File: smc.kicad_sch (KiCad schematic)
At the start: 46 parts, among them SW1 SW_Push, SW2 SW_Push, U5 W25Q128JVS, U6 RP2040, Y1 12MHz 20pF

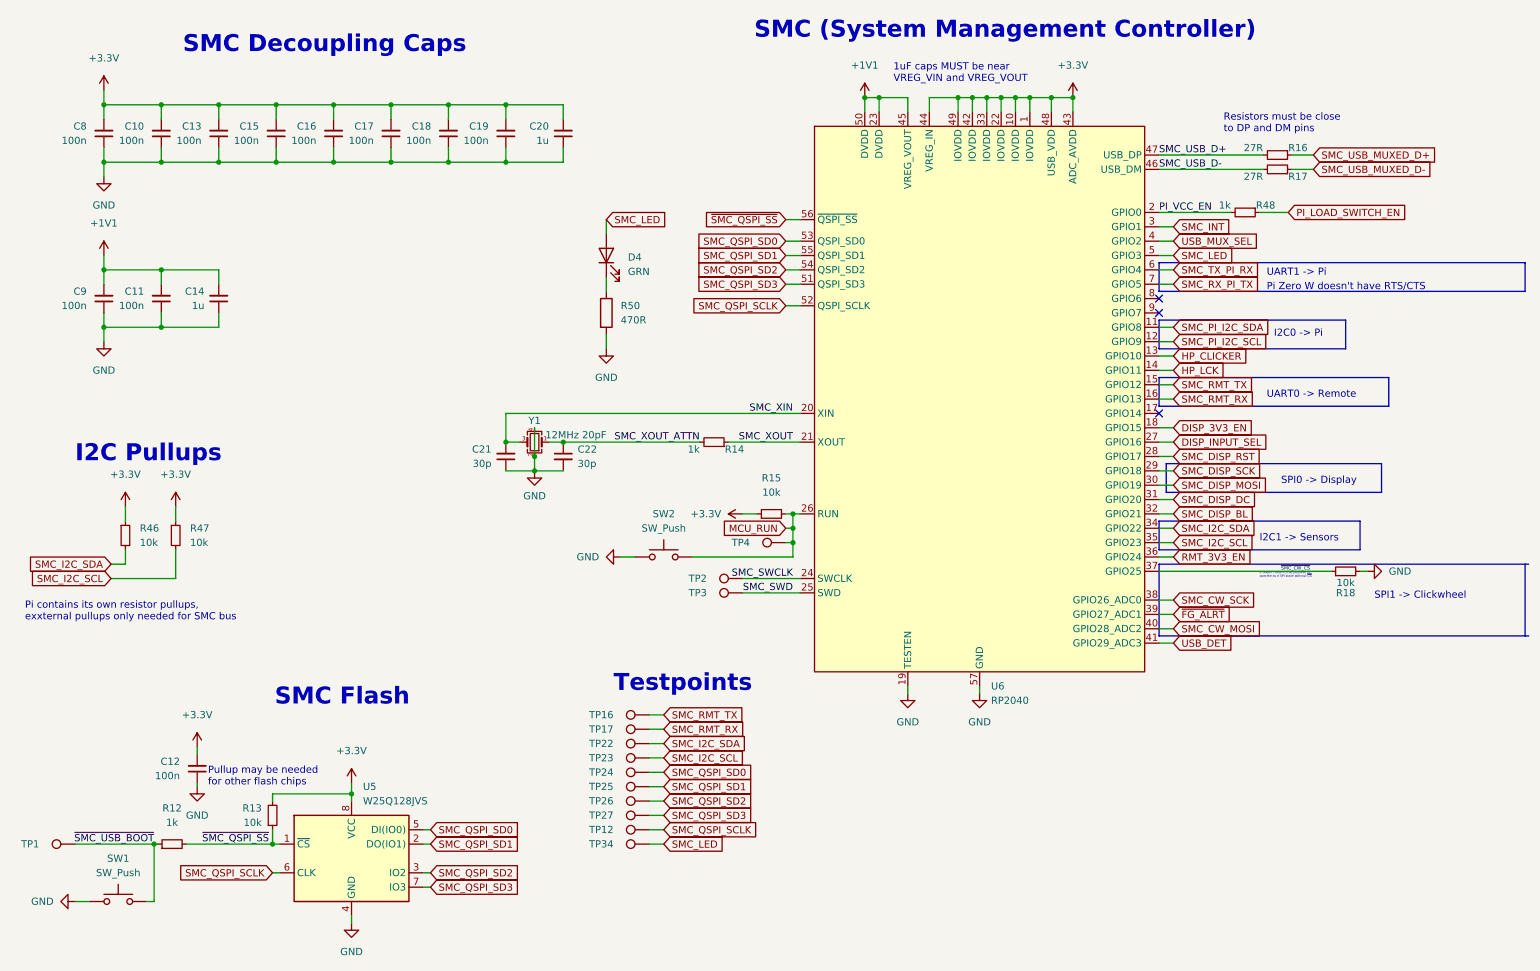
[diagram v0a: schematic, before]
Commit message: ci: test marking parts in sch for bom
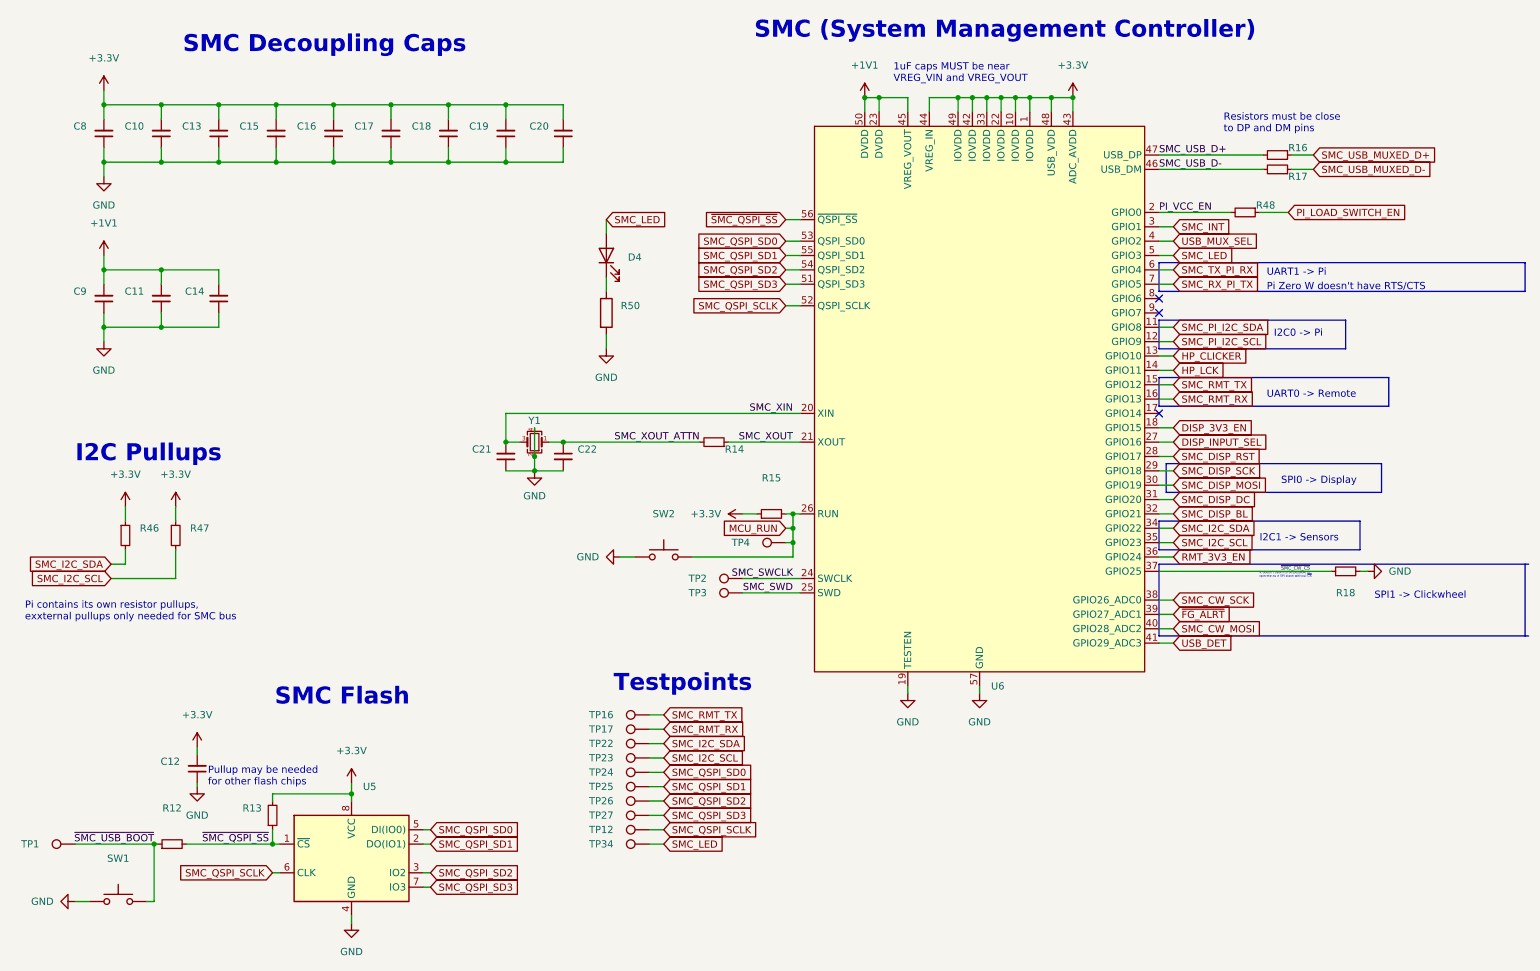
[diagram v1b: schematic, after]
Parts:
- C10, C11, C12, C13, C15, C16, C17, C18, C19, C8, C9: value 100n -> (none); footprint Capacitor_SMD:C_0402_1005Metric -> (none)
- C14, C20: value 1u -> (none); footprint Capacitor_SMD:C_0402_1005Metric -> (none)
- C21, C22: value 30p -> (none); footprint Capacitor_SMD:C_0402_1005Metric -> (none)
- D4: value GRN -> (none); footprint LED_SMD:LED_0402_1005Metric -> (none)
- R12, R14, R48: value 1k -> (none); footprint Resistor_SMD:R_0402_1005Metric -> (none)
- R13, R15, R18, R46, R47: value 10k -> (none); footprint Resistor_SMD:R_0402_1005Metric -> (none)
- R16, R17: value 27R -> (none); footprint Resistor_SMD:R_0402_1005Metric -> (none)
- R50: value 470R -> (none); footprint Resistor_SMD:R_0402_1005Metric -> (none)
- SW1, SW2: value SW_Push -> (none); footprint Gigahawk:SW_Push_1P1T_NO_CK_KMR2 -> (none)
- TP1, TP12, TP16, TP17, TP2, TP22, TP23, TP24, TP25, TP26, TP27, TP3, TP34, TP4: value TestPoint -> (none); footprint TestPoint:TestPoint_Pad_D1.5mm -> (none)
- U5: value W25Q128JVS -> (none); footprint Gigahawk:WSON-8-1EP_6x5mm_P1.27mm_EP3.4x4.3mm -> (none)
- U6: value RP2040 -> (none); footprint Package_DFN_QFN:QFN-56-1EP_7x7mm_P0.4mm_EP5.6x5.6mm -> (none); Mouser Part RPI Chip RP2040-7-500 -> RPI Chip RP2040-7-500
- Y1: value 12MHz 20pF -> (none); footprint Gigahawk:Crystal_SMD_2520-4Pin_2.5x2.0mm -> (none)
